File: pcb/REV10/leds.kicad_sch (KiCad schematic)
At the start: 35 parts

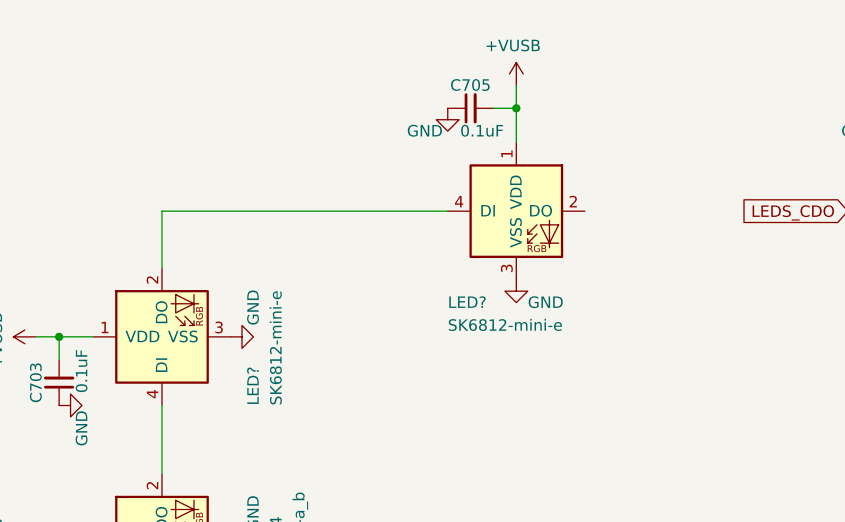
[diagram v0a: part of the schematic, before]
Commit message: REV10: add missing LED, fix LED placement.
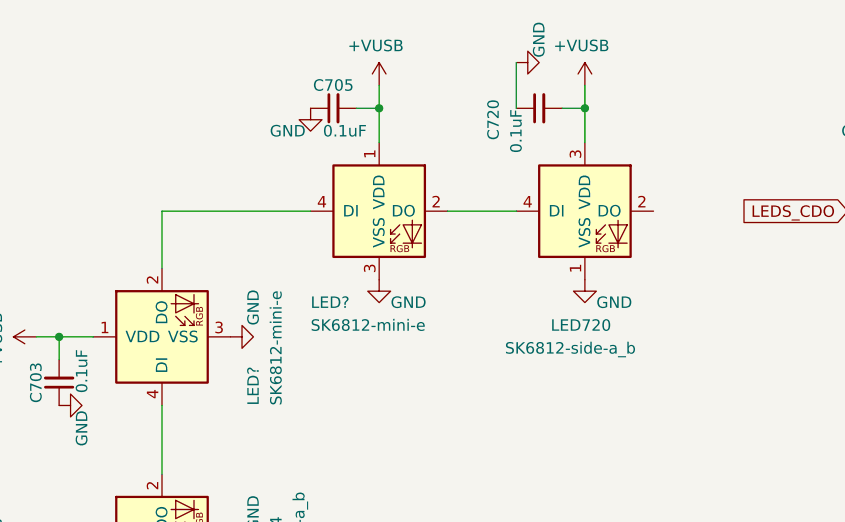
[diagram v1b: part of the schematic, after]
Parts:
- added C720: 0.1uF, Capacitor_SMD:C_0402_1005Metric, symbol Device:C_Small
- added LED720: SK6812-side-a_b, dp-LED:SK6812-side-a_b, symbol dp-LED:SK6812-side-a_b
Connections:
- net +VUSB: now also C720.2, LED720.3 (VDD)
- net GND: now also C720.1, LED720.1 (VSS)
- net at LED?.2 (DO): now also LED720.4 (DI)
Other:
- moved on the sheet: C705, LED?
